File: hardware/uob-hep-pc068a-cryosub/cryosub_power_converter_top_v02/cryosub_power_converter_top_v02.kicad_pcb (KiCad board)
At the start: 4 copper layers, 34 x 45 mm, 36 parts, among them J1 Conn_01x02_Male, J2 Conn_02x05_Odd_Even, J3 Conn_01x02_Male, Q1 IRLML2402TR, Q2 IRLML2402TR, Q3 FDD306P, U1 LT3042xMSE

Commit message: Tidied up silk. Produced Gerber/Drill files
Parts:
- moved C1 1.26 mm to (115.2, 138.8)
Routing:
- net VDC: track 29.8 -> 30.4 mm
- net /On When Warm/VD1: track 17.0 -> 16.5 mm

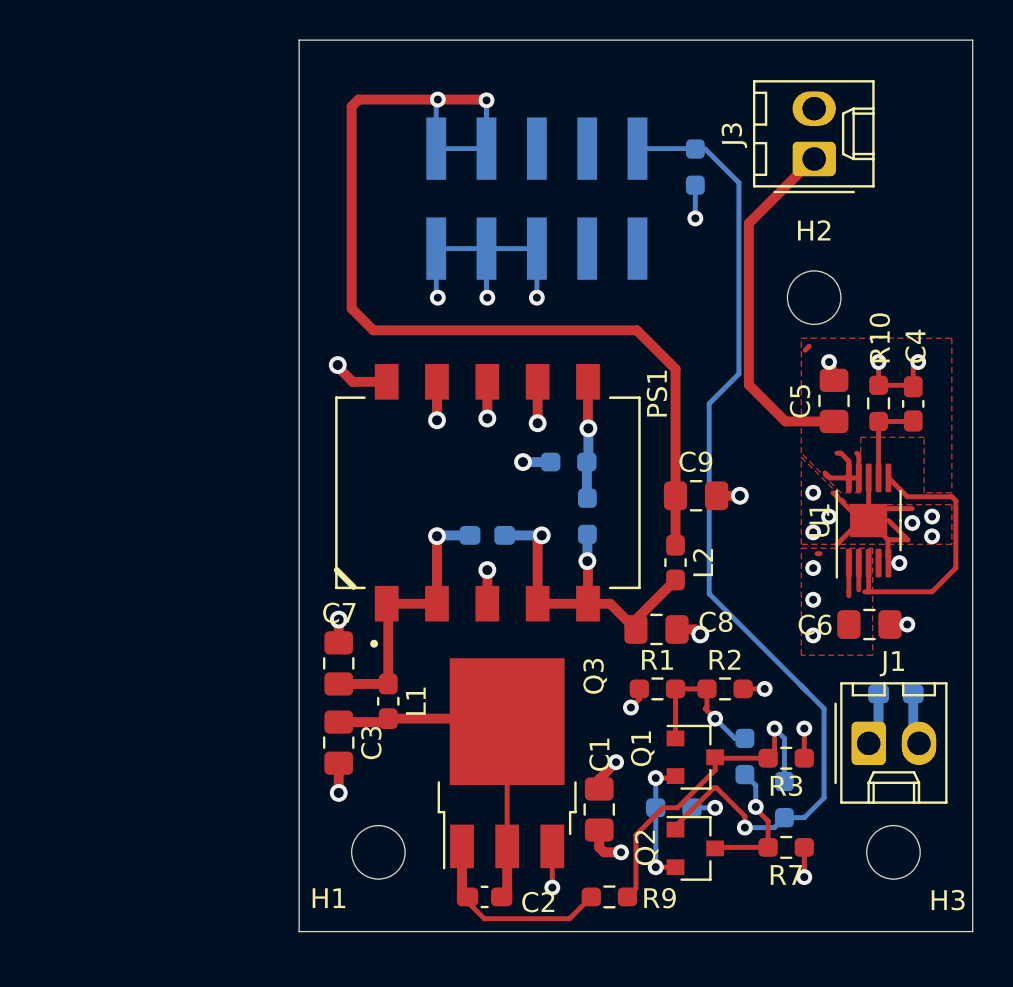
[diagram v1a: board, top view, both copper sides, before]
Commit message: Comitting version with 5V-->48V DC-DC converter
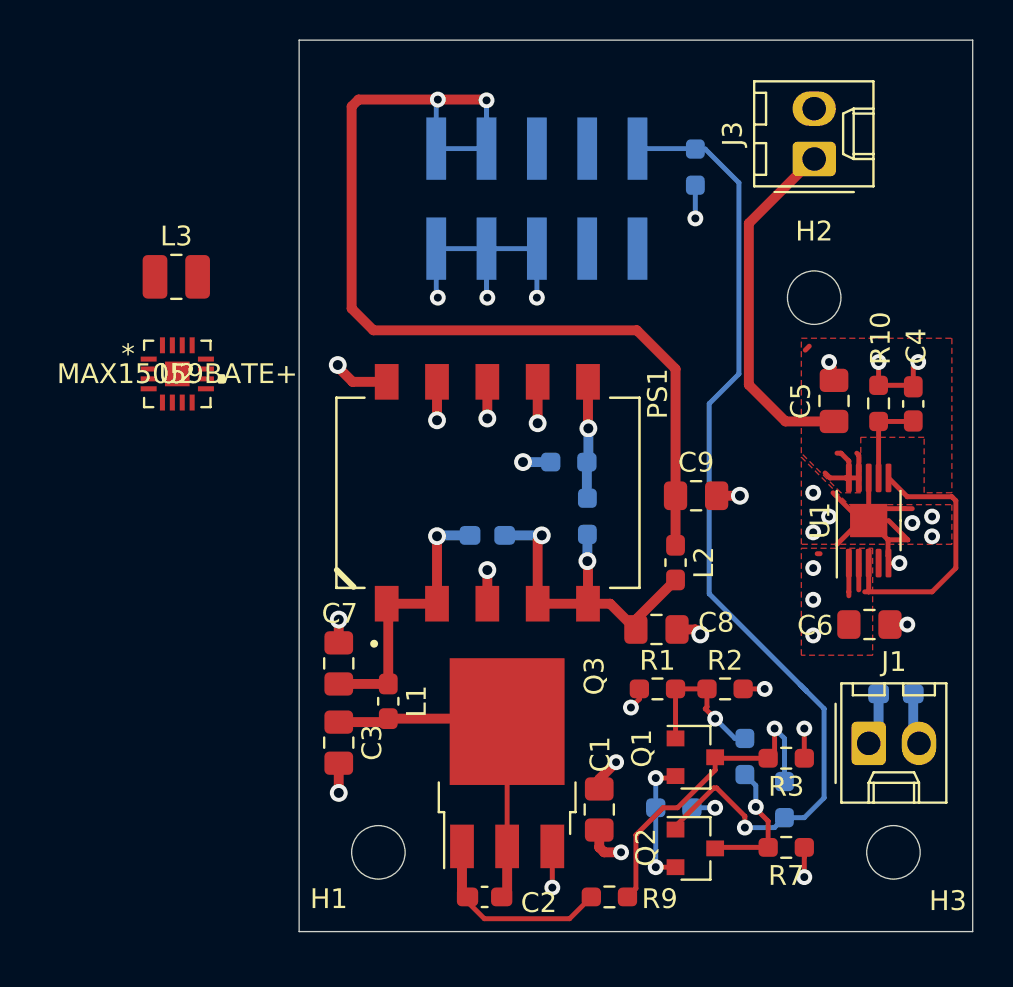
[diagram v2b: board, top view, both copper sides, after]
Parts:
- added L3: L, Inductor_SMD:L_1008_2520Metric, F.Cu at (93.8, 112.0)
- added U2: MAX15059BATE+, MAX15059BATET:MAX15059BATE&plus_, F.Cu at (93.8, 116.8)
